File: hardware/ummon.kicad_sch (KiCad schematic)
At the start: 95 parts, among them J1 Conn_01x08_Pin, J2 Conn_01x05_Pin, J3 Conn_01x04_Pin, J4 Conn_01x04_Pin, J5 Conn_01x04_Pin, P1 FPC 0.5MM 24P Vertical, Q1 SI1308EDL, SW1 Reboot, SW2 Flash, SW3 Test Button, U1 ESP32-C6-WROOM-1-N8, U2 SCD41-D-R2, U3 SGP41-D-R4, U4 SHT41-AD1B-R2, U5 AMS1117-3.3

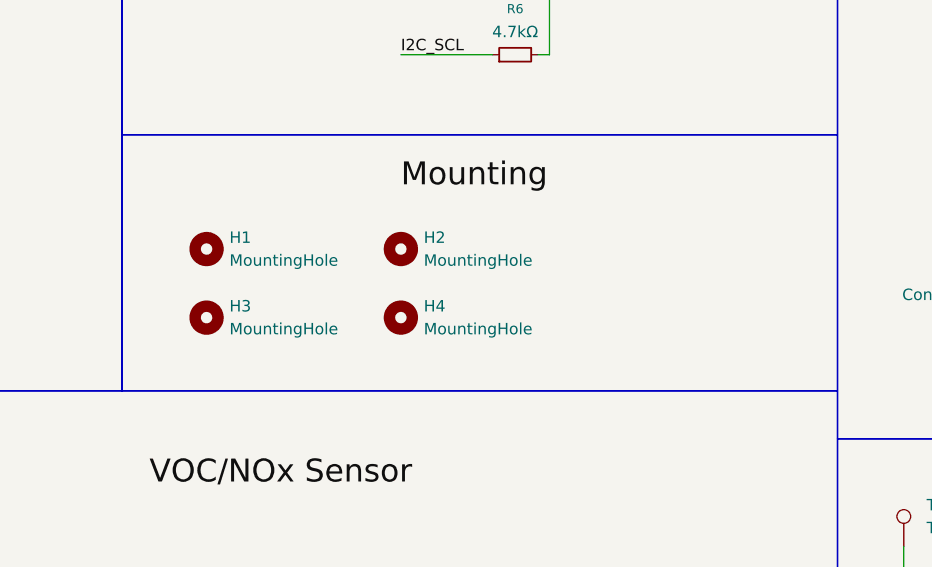
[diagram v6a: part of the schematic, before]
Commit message: :sparkles: Place ldo and route usb frontend
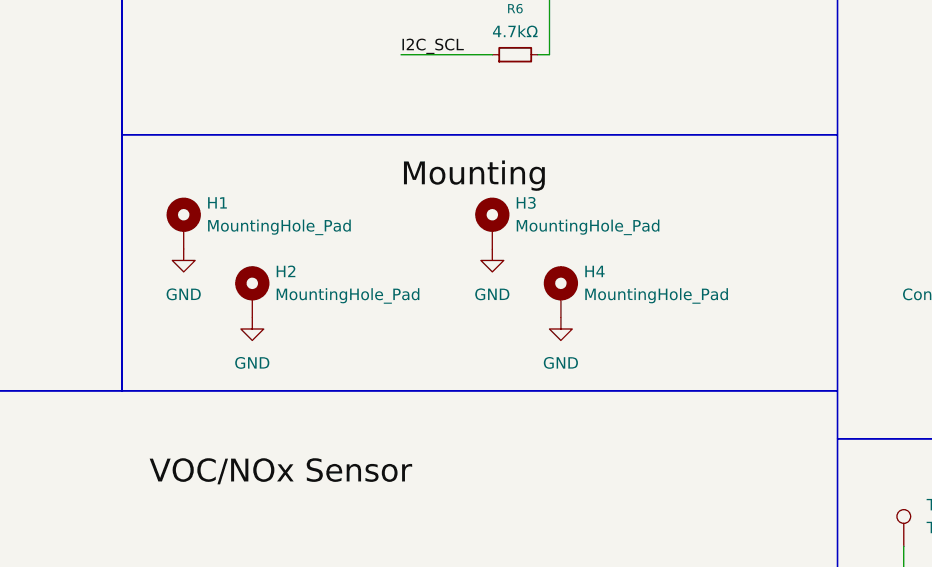
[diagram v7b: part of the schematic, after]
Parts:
- removed H1, H2, H3, H4: MountingHole, MountingHole:MountingHole_3.2mm_M3, symbol Mechanical:MountingHole
- added H1, H2, H3, H4: MountingHole_Pad, MountingHole:MountingHole_3.2mm_M3_Pad, symbol Mechanical:MountingHole_Pad
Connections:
- net GND: now also H1.1, H2.1, H3.1, H4.1

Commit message: :recycle: Replace RSE solder jumper with MSK12CO2 slide switch
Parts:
- removed H1: MountingHole_Pad, MountingHole:MountingHole_3.2mm_M3_Pad, symbol Mechanical:MountingHole_Pad
- removed JP2: RSE_Jumper, Jumper:SolderJumper-3_P1.3mm_Bridged12_RoundedPad1.0x1.5mm_NumberLabels, symbol Jumper:SolderJumper_3_Bridged12
- added H1: MountingHole, MountingHole:MountingHole_3.2mm_M3, symbol Mechanical:MountingHole
- added SW4: MINI MSK12CO2, parts:SW-SMD_MSK12CO2, symbol parts:MINIMSK12CO2
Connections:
- net EPD_RESE: now also SW4.2
- net GND: now also SW4.4, SW4.5
- net at R11.2, R13.2: now also SW4.3
- net at R10.2: now also SW4.1
